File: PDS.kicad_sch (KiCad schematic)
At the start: 8 parts, among them J1 MacSEPDS

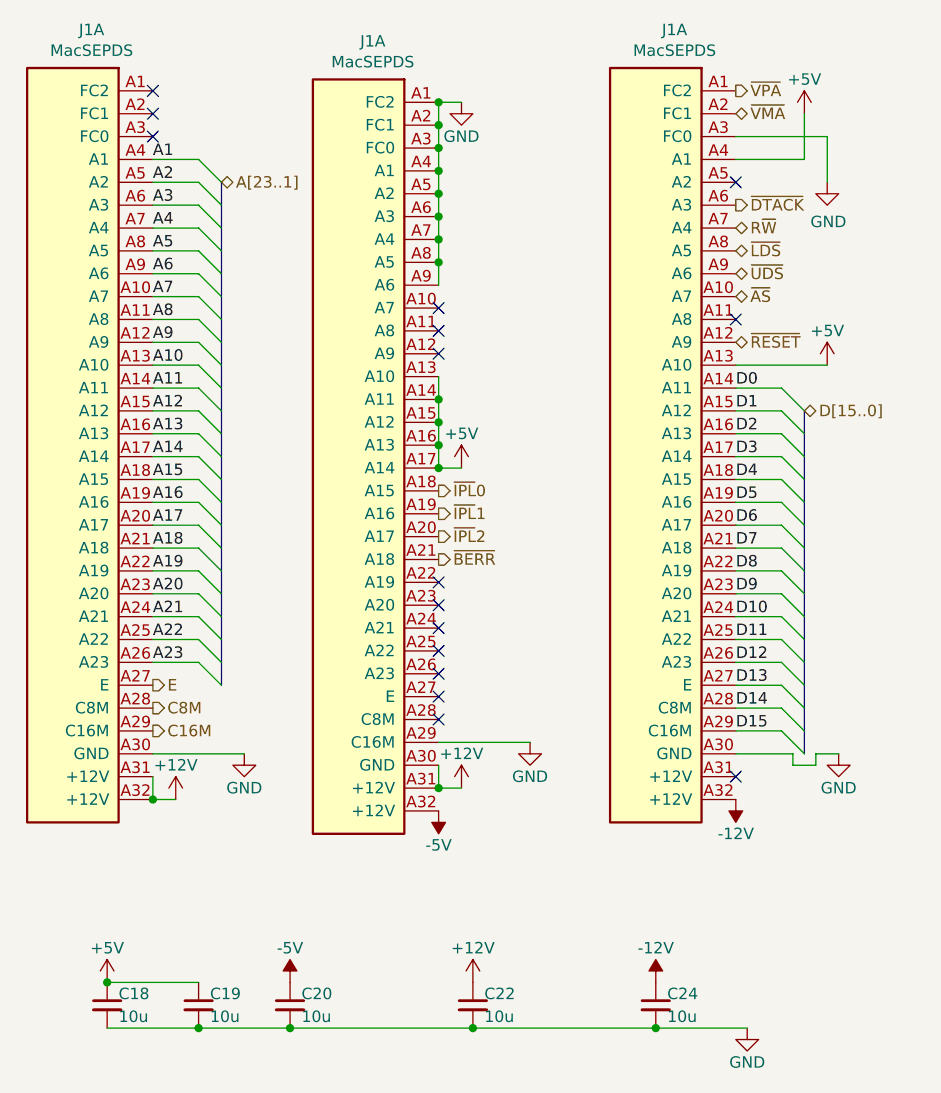
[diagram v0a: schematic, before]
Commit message: Migrate to KiCAD 6
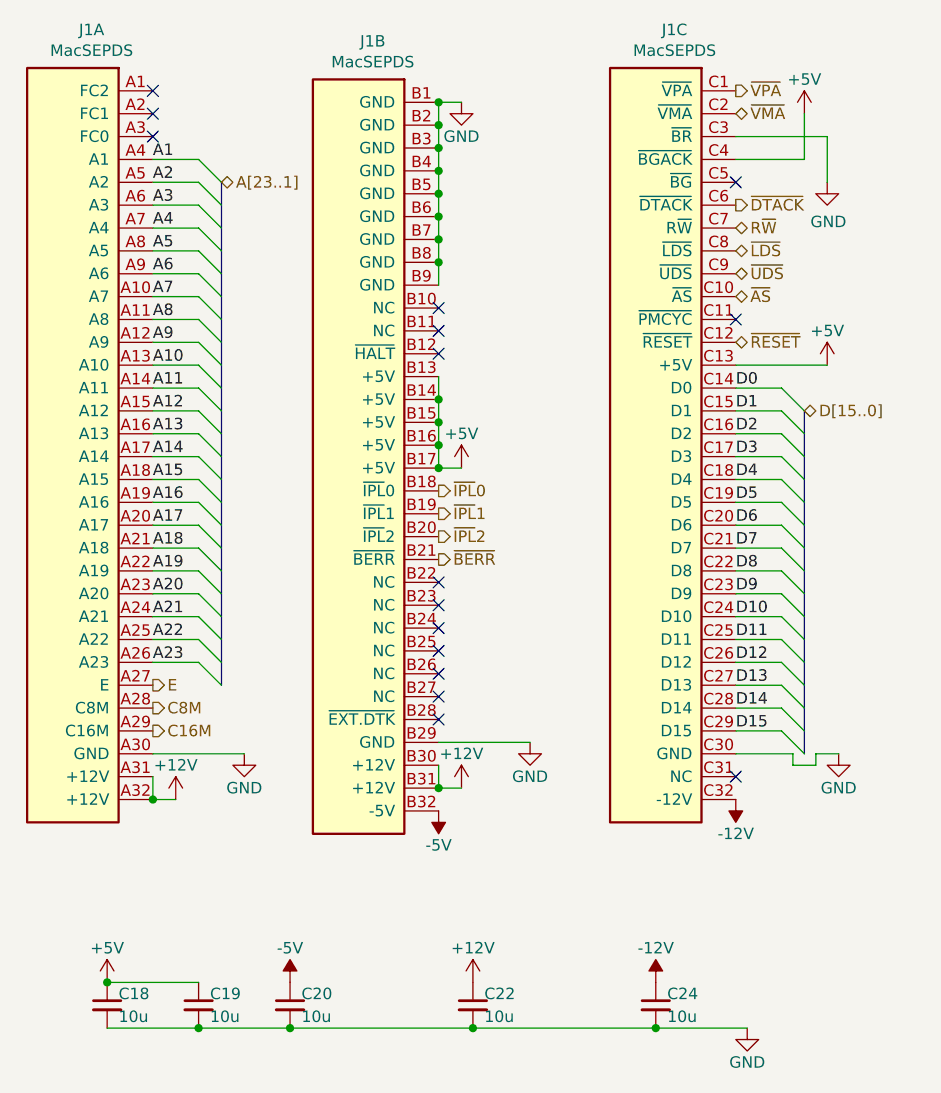
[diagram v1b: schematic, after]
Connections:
- net +12V: now also J1.B30 (+12V), J1.B31 (+12V); no longer J1.A30 (GND), J1.A31 (+12V)
- net +5V: now also J1.B13 (+5V), J1.B14 (+5V), J1.B15 (+5V), J1.B16 (+5V), J1.B17 (+5V), J1.C13 (+5V), J1.C4 (~{BGACK}); no longer J1.A13 (A10), J1.A13 (A10), J1.A14 (A11), J1.A15 (A12), J1.A16 (A13), J1.A17 (A14), J1.A4 (A1)
- net -12V: now also J1.C32 (-12V); no longer J1.A32 (+12V)
- net -5V: now also J1.B32 (-5V); no longer J1.A32 (+12V)
- net D0: now also J1.C14 (D0); no longer J1.A14 (A11)
- net D1: now also J1.C15 (D1); no longer J1.A15 (A12)
- net D10: now also J1.C24 (D10); no longer J1.A24 (A21)
- net D11: now also J1.C25 (D11); no longer J1.A25 (A22)
- net D12: now also J1.C26 (D12); no longer J1.A26 (A23)
- net D13: now also J1.C27 (D13); no longer J1.A27 (E)
- net D14: now also J1.C28 (D14); no longer J1.A28 (C8M)
- net D15: now also J1.C29 (D15); no longer J1.A29 (C16M)
- net D2: now also J1.C16 (D2); no longer J1.A16 (A13)
- net D3: now also J1.C17 (D3); no longer J1.A17 (A14)
- net D4: now also J1.C18 (D4); no longer J1.A18 (A15)
- net D5: now also J1.C19 (D5); no longer J1.A19 (A16)
- net D6: now also J1.C20 (D6); no longer J1.A20 (A17)
- net D7: now also J1.C21 (D7); no longer J1.A21 (A18)
- net D8: now also J1.C22 (D8); no longer J1.A22 (A19)
- net D9: now also J1.C23 (D9); no longer J1.A23 (A20)
- net GND: now also J1.B1 (GND), J1.B2 (GND), J1.B29 (GND), J1.B3 (GND), J1.B4 (GND), J1.B5 (GND), J1.B6 (GND), J1.B7 (GND), J1.B8 (GND), J1.B9 (GND), J1.C3 (~{BR}), J1.C30 (GND); no longer J1.A1 (FC2), J1.A2 (FC1), J1.A29 (C16M), J1.A3 (FC0), J1.A3 (FC0), J1.A30 (GND), J1.A4 (A1), J1.A5 (A2), J1.A6 (A3), J1.A7 (A4), J1.A8 (A5), J1.A9 (A6)
- net R~{W}: now also J1.C7 (R~{W}); no longer J1.A7 (A4)
- net ~{AS}: now also J1.C10 (~{AS}); no longer J1.A10 (A7)
- net ~{BERR}: now also J1.B21 (~{BERR}); no longer J1.A21 (A18)
- net ~{DTACK}: now also J1.C6 (~{DTACK}); no longer J1.A6 (A3)
- net ~{IPL}0: now also J1.B18 (~{IPL}0); no longer J1.A18 (A15)
- net ~{IPL}1: now also J1.B19 (~{IPL}1); no longer J1.A19 (A16)
- net ~{IPL}2: now also J1.B20 (~{IPL}2); no longer J1.A20 (A17)
- net ~{LDS}: now also J1.C8 (~{LDS}); no longer J1.A8 (A5)
- net ~{RESET}: now also J1.C12 (~{RESET}); no longer J1.A12 (A9)
- net ~{UDS}: now also J1.C9 (~{UDS}); no longer J1.A9 (A6)
- net ~{VMA}: now also J1.C2 (~{VMA}); no longer J1.A2 (FC1)
- net ~{VPA}: now also J1.C1 (~{VPA}); no longer J1.A1 (FC2)
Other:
- moved on the sheet: J1B, J1C
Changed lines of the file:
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@@
     (effects (font (size 1.27 1.27)) (justify left))
   )
-  (symbol (lib_id "GW_Connector:MacSEPDS") (at 34.29 100.33 0)
+  (symbol (lib_id "GW_Connector:MacSEPDS") (at 34.29 100.33 0) (unit 1)
     (in_bom yes) (on_board yes)
     (property "Reference" "J1" (id 0) (at 31.2928 51.6382 0))
@@
     (pin "A9")
   )
-  (symbol (lib_id "GW_Connector:MacSEPDS") (at 66.04 101.6 0)
+  (symbol (lib_id "GW_Connector:MacSEPDS") (at 66.04 101.6 0) (unit 2)
     (in_bom yes) (on_board yes)
     (property "Reference" "J1" (id 0) (at 62.5348 52.9082 0))
@@
     (pin "B9")
   )
-  (symbol (lib_id "GW_Connector:MacSEPDS") (at 99.06 100.33 0)
+  (symbol (lib_id "GW_Connector:MacSEPDS") (at 99.06 100.33 0) (unit 3)
     (in_bom yes) (on_board yes)
     (property "Reference" "J1" (id 0) (at 96.0628 51.6382 0))
@@
     (pin "1")
   )
-  (symbol (lib_id "Device:C_Small") (at 53.34 160.02 0)
+  (symbol (lib_id "Device:C_Small") (at 53.34 160.02 0) (unit 1)
     (in_bom yes) (on_board yes)
     (property "Reference" "C20" (id 0) (at 54.61 158.75 0)
@@
     (pin "2")
   )
-  (symbol (lib_id "Device:C_Small") (at 43.18 160.02 0)
+  (symbol (lib_id "Device:C_Small") (at 43.18 160.02 0) (unit 1)
     (in_bom yes) (on_board yes)
     (property "Reference" "C19" (id 0) (at 44.45 158.75 0)
@@
     (pin "2")
   )
-  (symbol (lib_id "Device:C_Small") (at 73.66 160.02 0)
+  (symbol (lib_id "Device:C_Small") (at 73.66 160.02 0) (unit 1)
     (in_bom yes) (on_board yes)
     (property "Reference" "C22" (id 0) (at 74.93 158.75 0)
@@
     (pin "2")
   )
-  (symbol (lib_id "Device:C_Small") (at 33.02 160.02 0)
+  (symbol (lib_id "Device:C_Small") (at 33.02 160.02 0) (unit 1)
     (in_bom yes) (on_board yes)
     (property "Reference" "C18" (id 0) (at 34.29 158.75 0)
@@
     (pin "1")
   )
-  (symbol (lib_id "power:GND") (at 104.14 162.56 0) (mirror y)
+  (symbol (lib_id "power:GND") (at 104.14 162.56 0) (mirror y) (unit 1)
     (in_bom yes) (on_board yes)
     (property "Reference" "#PWR0153" (id 0) (at 104.14 168.91 0)
@@
     (pin "1")
   )
-  (symbol (lib_id "Device:C_Small") (at 93.98 160.02 0)
+  (symbol (lib_id "Device:C_Small") (at 93.98 160.02 0) (unit 1)
     (in_bom yes) (on_board yes)
     (property "Reference" "C24" (id 0) (at 95.25 158.75 0)

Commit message: idk
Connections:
- net +5V: no longer J1.C4 (~{BGACK})
- no-connect marks 16 -> 17
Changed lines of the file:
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@@
   )
   (no_connect (at 69.85 85.09))
+  (no_connect (at 102.87 66.04))
   (no_connect (at 69.85 82.55))
   (no_connect (at 69.85 123.19))
@@
     (stroke (width 0) (type default) (color 0 0 0 0))
   )
-  (wire (pts (xy 111.76 133.35) (xy 111.76 132.08))
-    (stroke (width 0) (type default) (color 0 0 0 0))
-  )
   (wire (pts (xy 38.1 114.3) (xy 43.18 114.3))
     (stroke (width 0) (type default) (color 0 0 0 0))
@@
     (stroke (width 0) (type default) (color 0 0 0 0))
   )
-  (wire (pts (xy 111.76 132.08) (xy 114.3 132.08))
-    (stroke (width 0) (type default) (color 0 0 0 0))
-  )
   (wire (pts (xy 38.1 66.04) (xy 43.18 66.04))
     (stroke (width 0) (type default) (color 0 0 0 0))
@@
     (stroke (width 0) (type default) (color 0 0 0 0))
   )
-  (wire (pts (xy 48.26 132.08) (xy 38.1 132.08))
+  (wire (pts (xy 45.72 132.08) (xy 38.1 132.08))
     (stroke (width 0) (type default) (color 0 0 0 0))
   )
@@
     (stroke (width 0) (type default) (color 0 0 0 0))
   )
-  (wire (pts (xy 102.87 132.08) (xy 109.22 132.08))
+  (wire (pts (xy 102.87 132.08) (xy 105.41 132.08))
     (stroke (width 0) (type default) (color 0 0 0 0))
   )
@@
     (stroke (width 0) (type default) (color 0 0 0 0))
   )
-  (wire (pts (xy 109.22 133.35) (xy 111.76 133.35))
-    (stroke (width 0) (type default) (color 0 0 0 0))
-  )
   (bus (pts (xy 45.72 83.82) (xy 45.72 86.36))
     (stroke (width 0) (type default) (color 0 0 0 0))
@@
     (stroke (width 0) (type default) (color 0 0 0 0))
   )
-  (wire (pts (xy 102.87 66.04) (xy 110.49 66.04))
-    (stroke (width 0) (type default) (color 0 0 0 0))
-  )
   (wire (pts (xy 102.87 127) (xy 107.95 127))
     (stroke (width 0) (type default) (color 0 0 0 0))
@@
     (stroke (width 0) (type default) (color 0 0 0 0))
   )
-  (wire (pts (xy 109.22 132.08) (xy 109.22 133.35))
-    (stroke (width 0) (type default) (color 0 0 0 0))
-  )
   (wire (pts (xy 102.87 119.38) (xy 107.95 119.38))
     (stroke (width 0) (type default) (color 0 0 0 0))
@@
     (stroke (width 0) (type default) (color 0 0 0 0))
   )
-  (wire (pts (xy 80.01 130.81) (xy 69.85 130.81))
+  (wire (pts (xy 77.47 130.81) (xy 69.85 130.81))
     (stroke (width 0) (type default) (color 0 0 0 0))
   )
@@
   )
   (bus (pts (xy 110.49 121.92) (xy 110.49 124.46))
-    (stroke (width 0) (type default) (color 0 0 0 0))
-  )
-  (wire (pts (xy 110.49 66.04) (xy 110.49 60.96))
     (stroke (width 0) (type default) (color 0 0 0 0))
   )
@@
     (pin "1")
   )
-  (symbol (lib_id "power:GND") (at 114.3 132.08 0) (unit 1)
-    (in_bom yes) (on_board yes)
-    (property "Reference" "#PWR0146" (id 0) (at 114.3 138.43 0)
-      (effects (font (size 1.27 1.27)) hide)
-    )
-    (property "Value" "GND" (id 1) (at 114.3 135.89 0))
-    (property "Footprint" "" (id 2) (at 114.3 132.08 0)
-      (effects (font (size 1.27 1.27)) hide)
-    )
-    (property "Datasheet" "" (id 3) (at 114.3 132.08 0)
-      (effects (font (size 1.27 1.27)) hide)
-    )
-    (pin "1")
-  )
-  (symbol (lib_id "power:GND") (at 48.26 132.08 0) (unit 1)
-    (in_bom yes) (on_board yes)
-    (property "Reference" "#PWR0147" (id 0) (at 48.26 138.43 0)
-      (effects (font (size 1.27 1.27)) hide)
-    )
-    (property "Value" "GND" (id 1) (at 48.26 135.89 0))
-    (property "Footprint" "" (id 2) (at 48.26 132.08 0)
-      (effects (font (size 1.27 1.27)) hide)
-    )
-    (property "Datasheet" "" (id 3) (at 48.26 132.08 0)
+  (symbol (lib_id "power:GND") (at 105.41 132.08 0) (unit 1)
+    (in_bom yes) (on_board yes)
+    (property "Reference" "#PWR0146" (id 0) (at 105.41 138.43 0)
+      (effects (font (size 1.27 1.27)) hide)
+    )
+    (property "Value" "GND" (id 1) (at 105.41 135.89 0))
+    (property "Footprint" "" (id 2) (at 105.41 132.08 0)
+      (effects (font (size 1.27 1.27)) hide)
+    )
+    (property "Datasheet" "" (id 3) (at 105.41 132.08 0)
+      (effects (font (size 1.27 1.27)) hide)
+    )
+    (pin "1")
+  )
+  (symbol (lib_id "power:GND") (at 45.72 132.08 0) (unit 1)
+    (in_bom yes) (on_board yes)
+    (property "Reference" "#PWR0147" (id 0) (at 45.72 138.43 0)
+      (effects (font (size 1.27 1.27)) hide)
+    )
+    (property "Value" "GND" (id 1) (at 45.72 135.89 0))
+    (property "Footprint" "" (id 2) (at 45.72 132.08 0)
+      (effects (font (size 1.27 1.27)) hide)
+    )
+    (property "Datasheet" "" (id 3) (at 45.72 132.08 0)
       (effects (font (size 1.27 1.27)) hide)
     )
@@
     (pin "1")
   )
-  (symbol (lib_id "power:GND") (at 80.01 130.81 0) (unit 1)
-    (in_bom yes) (on_board yes)
-    (property "Reference" "#PWR0149" (id 0) (at 80.01 137.16 0)
-      (effects (font (size 1.27 1.27)) hide)
-    )
-    (property "Value" "GND" (id 1) (at 80.01 134.62 0))
-    (property "Footprint" "" (id 2) (at 80.01 130.81 0)
-      (effects (font (size 1.27 1.27)) hide)
-    )
-    (property "Datasheet" "" (id 3) (at 80.01 130.81 0)
+  (symbol (lib_id "power:GND") (at 77.47 130.81 0) (unit 1)
+    (in_bom yes) (on_board yes)
+    (property "Reference" "#PWR0149" (id 0) (at 77.47 137.16 0)
+      (effects (font (size 1.27 1.27)) hide)
+    )
+    (property "Value" "GND" (id 1) (at 77.47 134.62 0))
+    (property "Footprint" "" (id 2) (at 77.47 130.81 0)
+      (effects (font (size 1.27 1.27)) hide)
+    )
+    (property "Datasheet" "" (id 3) (at 77.47 130.81 0)
       (effects (font (size 1.27 1.27)) hide)
     )
@@
       (effects (font (size 1.27 1.27)) hide)
     )
-    (property "Value" "GND" (id 1) (at 113.157 72.9742 0))
+    (property "Value" "GND" (id 1) (at 113.03 72.39 0))
     (property "Footprint" "" (id 2) (at 113.03 68.58 0)
       (effects (font (size 1.27 1.27)) hide)
@@
       (effects (font (size 1.27 1.27)) hide)
     )
-    (pin "1")
-  )
-  (symbol (lib_id "power:+5V") (at 110.49 60.96 0) (unit 1)
-    (in_bom yes) (on_board yes)
-    (property "Reference" "#PWR0157" (id 0) (at 110.49 64.77 0)
-      (effects (font (size 1.27 1.27)) hide)
-    )
-    (property "Value" "+5V" (id 1) (at 110.49 57.15 0))
-    (property "Footprint" "" (id 2) (at 110.49 60.96 0)
-      (effects (font (size 1.27 1.27)) hide)
-    )
-    (property "Datasheet" "" (id 3) (at 110.49 60.96 0)
-      (effects (font (size 1.27 1.27)) hide)
-    )

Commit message: Prototype
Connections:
- net GND: no longer J1.C3 (~{BR})
- net ~{BG}: now reaches J1.C5 (~{BG})
- new net ~{BR}: J1.C3 (~{BR})
- no-connect marks 17 -> 16
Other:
- moved on the sheet: J1B

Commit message: RC
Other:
- company: (none) -> Garrett's Workshop
- title: (none) -> WarpSE (GW4410A)
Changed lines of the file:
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@@
 (kicad_sch (version 20230121) (generator eeschema)
   (paper "A4")
+  (title_block
+    (title "WarpSE (GW4410A)")
+    (date "2024-03-27")
+    (rev "1.0")
+    (company "Garrett's Workshop")
+  )
   (junction (at 72.39 91.44) (diameter 0) (color 0 0 0 0)
   )

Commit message: USB power
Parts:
- removed C19: 10u, stdpads:C_0805, symbol Device:C_Small
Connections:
- net +5V renamed +5Vin

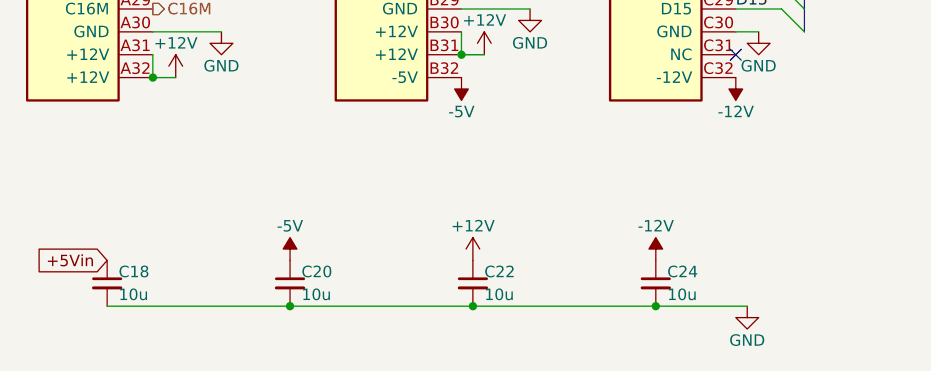
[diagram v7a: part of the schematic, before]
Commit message: Board prerelease revision 3 with USB power, A[23:20] remapping
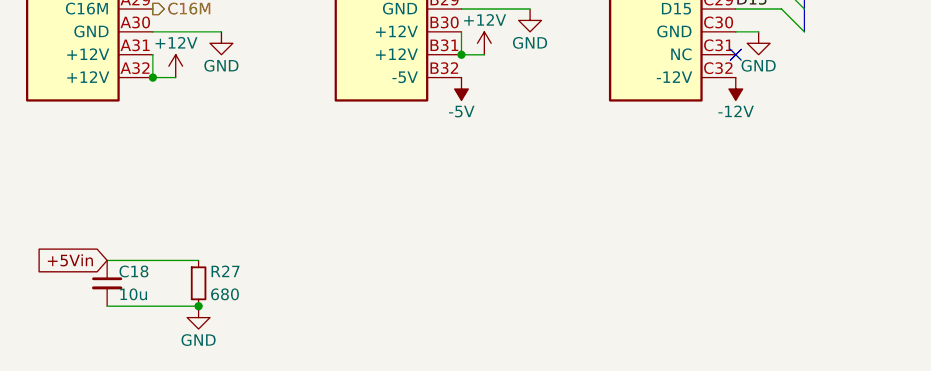
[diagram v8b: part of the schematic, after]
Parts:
- removed C20, C22, C24: 10u, stdpads:C_0805, symbol Device:C_Small
- added R27: 680, stdpads:R_0805, symbol Device:R_Small
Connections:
- net +5Vin: now also R27.1
- net GND: now also R27.2
